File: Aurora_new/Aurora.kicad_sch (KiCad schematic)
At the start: 0 parts

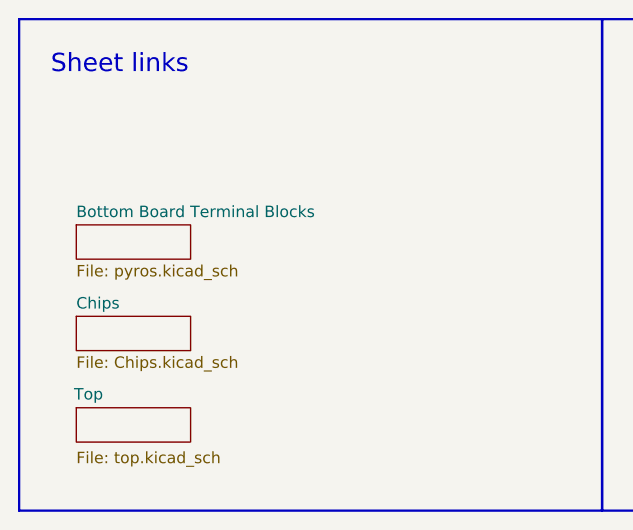
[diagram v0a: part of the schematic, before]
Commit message: added new regulator chain + rationale
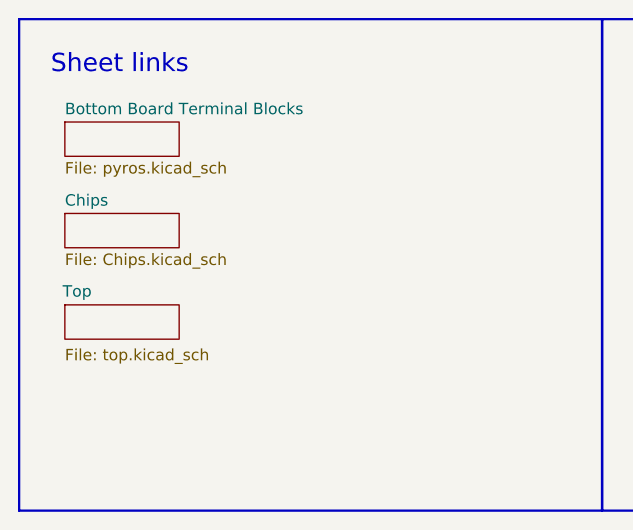
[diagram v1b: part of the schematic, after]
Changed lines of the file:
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@@
 	)
 	(sheet
-		(at 19.05 55.88)
+		(at 17.78 44.45)
 		(size 12.7 3.81)
 		(exclude_from_sim no)
@@
 		)
 		(property "Sheetname" "Top"
-			(at 18.796 55.118 0)
+			(at 17.526 43.688 0)
 			(effects
 				(font
@@
 		)
 		(property "Sheetfile" "top.kicad_sch"
-			(at 19.05 60.706 0)
+			(at 17.78 49.276 0)
 			(effects
 				(font
@@
 	)
 	(sheet
-		(at 19.05 45.72)
+		(at 17.78 34.29)
 		(size 12.7 3.81)
 		(exclude_from_sim no)
@@
 		)
 		(property "Sheetname" "Chips"
-			(at 19.05 45.0084 0)
+			(at 17.78 33.5784 0)
 			(effects
 				(font
@@
 		)
 		(property "Sheetfile" "Chips.kicad_sch"
-			(at 19.05 50.1146 0)
+			(at 17.78 38.6846 0)
 			(effects
 				(font
@@
 	)
 	(sheet
-		(at 19.05 35.56)
+		(at 17.78 24.13)
 		(size 12.7 3.81)
 		(exclude_from_sim no)
@@
 		)
 		(property "Sheetname" "Bottom Board Terminal Blocks"
-			(at 19.05 34.8484 0)
+			(at 17.78 23.4184 0)
 			(effects
 				(font
@@
 		)
 		(property "Sheetfile" "pyros.kicad_sch"
-			(at 19.05 39.9546 0)
+			(at 17.78 28.5246 0)
 			(effects
 				(font

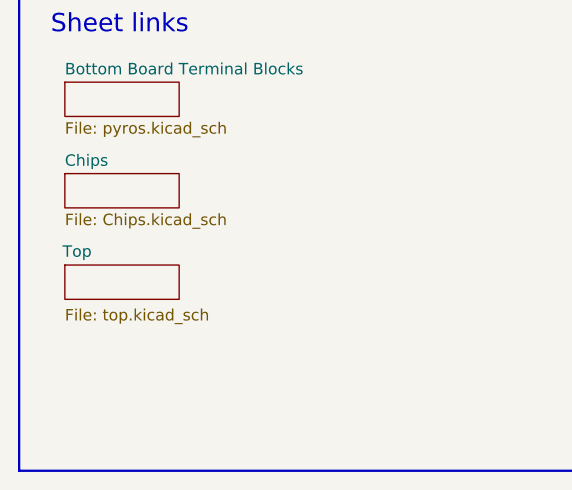
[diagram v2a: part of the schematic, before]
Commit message: fixed schematic issues, started organizing components in PCB
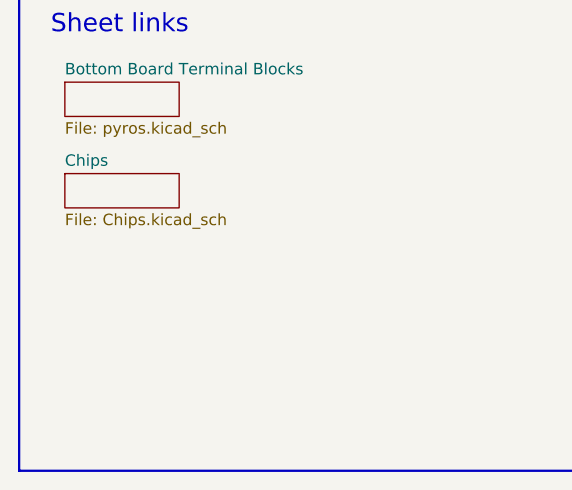
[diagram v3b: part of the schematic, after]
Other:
- removed sheet Top
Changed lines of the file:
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@@
-	)
-	(sheet
-		(at 17.78 44.45)
-		(size 12.7 3.81)
-		(exclude_from_sim no)
-		(in_bom yes)
-		(on_board yes)
-		(dnp no)
-		(stroke
-			(width 0.1524)
-			(type solid)
-		)
-		(fill
-			(color 0 0 0 0.0000)
-		)
-		(property "Sheetname" "Top"
-			(at 17.526 43.688 0)
-			(effects
-				(font
-					(size 1.27 1.27)
-				)
-				(justify left bottom)
-			)
-		)
-		(property "Sheetfile" "top.kicad_sch"
-			(at 17.78 49.276 0)
-			(effects
-				(font
-					(size 1.27 1.27)
-				)
-				(justify left top)
-			)
-		)
-		(instances
-			(project "Aurora"
-				(path "/073f53a3-faa8-4419-bff2-f325850469a4"
-					(page "4")
-				)
-			)
-		)
 	)
 	(sheet
